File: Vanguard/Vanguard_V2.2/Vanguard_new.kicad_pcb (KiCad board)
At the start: 4 copper layers, 50 x 41.2 mm, 77 parts, among them J1 USB_C_Receptacle_USB2.0_16P, J2 Conn_02x03_Pin, J3 Micro_SD_Card_Det1, J4 STARBOARD_SERVO, J5 PORTSIDE_SERVO, J6 Conn_01x02_Pin, J7 EJECTION_SERVO, Q1 BSS138, Q2 BSS138, Q3 BSS138, Q4 BSS138, U1 ATSAMD11D14A-M, U2 ATmega4809-A, U3 AT25DF641A-SH-T, U4 AP2112K-3.3, U5 BD1020HFV, U6 BNO086, U7 TXB0104D, U8 TPS61092, U9 MPM3610AGQV-P, Y1 32.768kHz

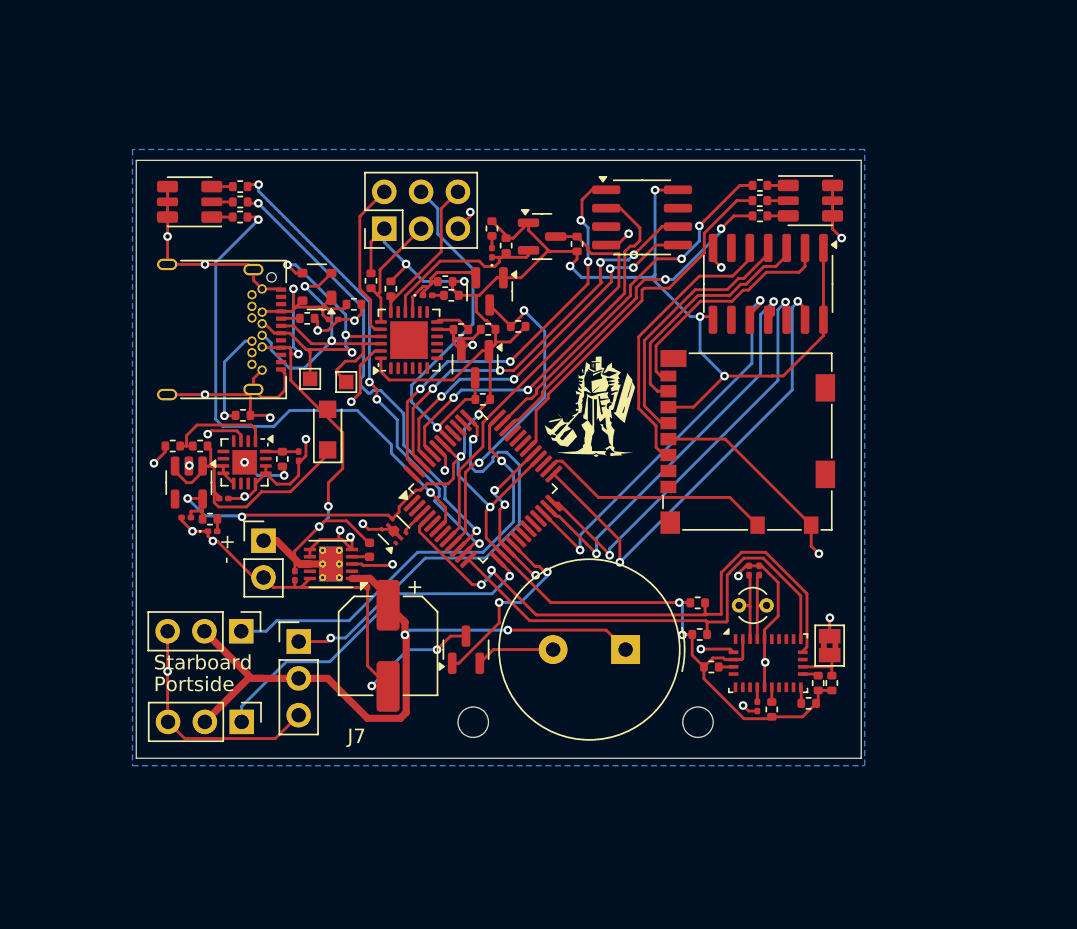
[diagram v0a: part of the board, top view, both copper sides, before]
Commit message: ground tracing improved
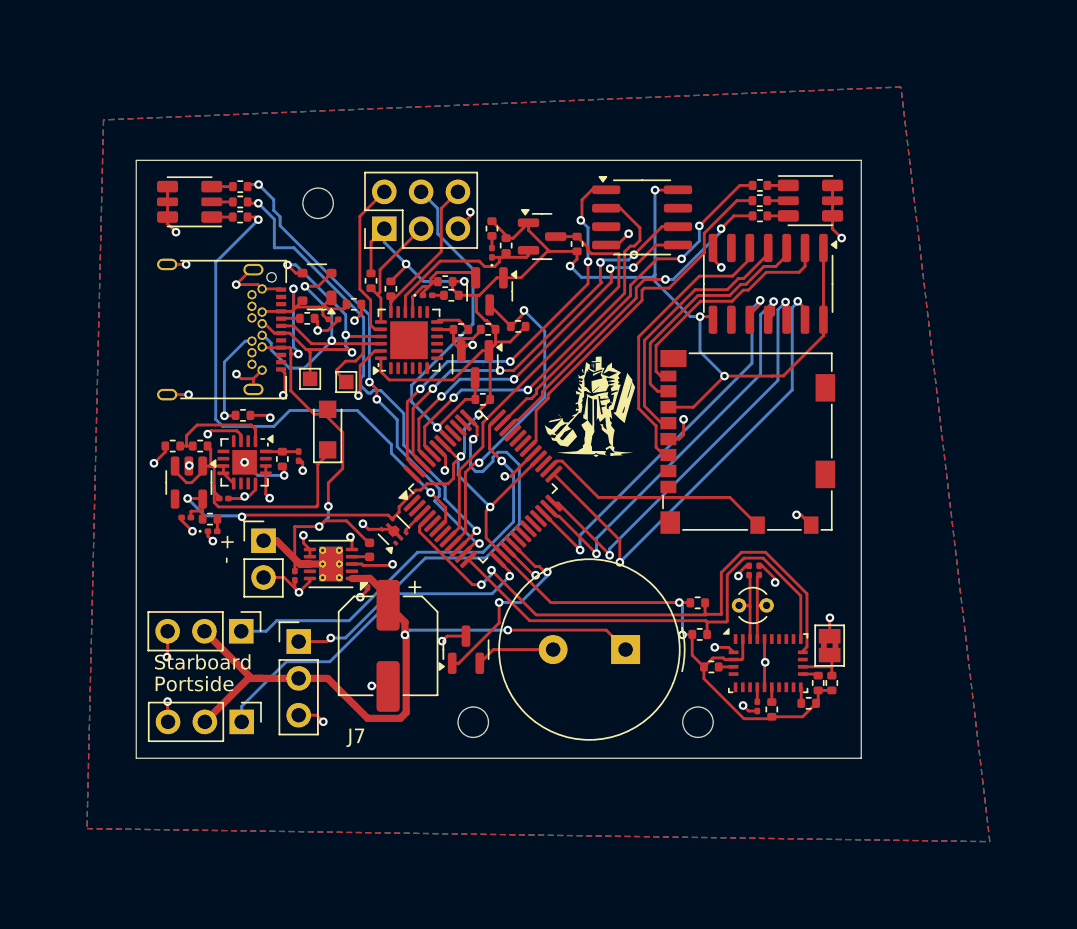
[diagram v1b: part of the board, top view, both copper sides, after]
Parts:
- added REF**: MountingHole_2.1mm, MountingHole:MountingHole_2.1mm, F.Cu at (154.8, 96.2)
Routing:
- net GND: track 165.9 -> 89.0 mm, vias 35 -> 44
- net Net-(D6-K): track 21.0 -> 22.6 mm
- net Net-(D1-GND): track 46.1 -> 47.5 mm
- net STAR_RED: track 32.3 -> 33.1 mm
- removed copper zone on B.Cu, net GND
